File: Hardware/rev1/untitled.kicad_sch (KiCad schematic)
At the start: 16 parts, among them J2 USB_C_Receptacle_USB2.0_14P, J3 Screw_Terminal_01x02, U2 HT75xx-1-SOT89

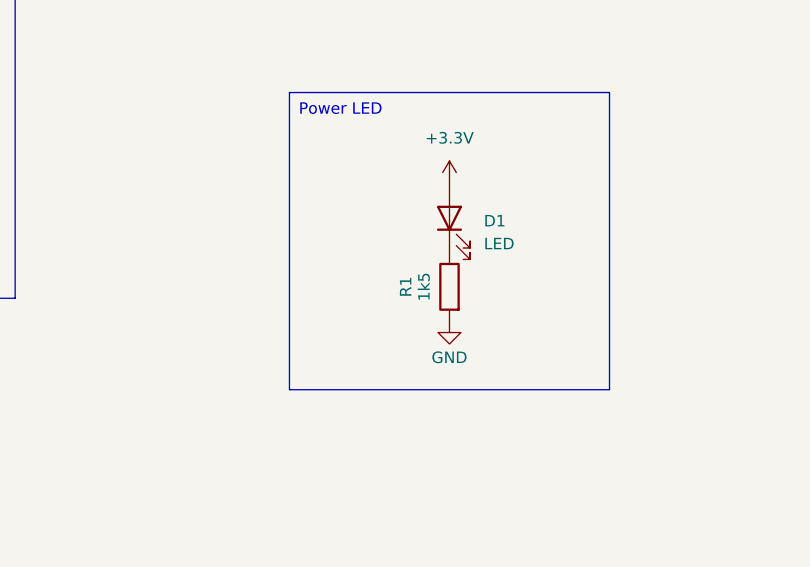
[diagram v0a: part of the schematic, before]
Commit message: Finish schematics, assign footprints
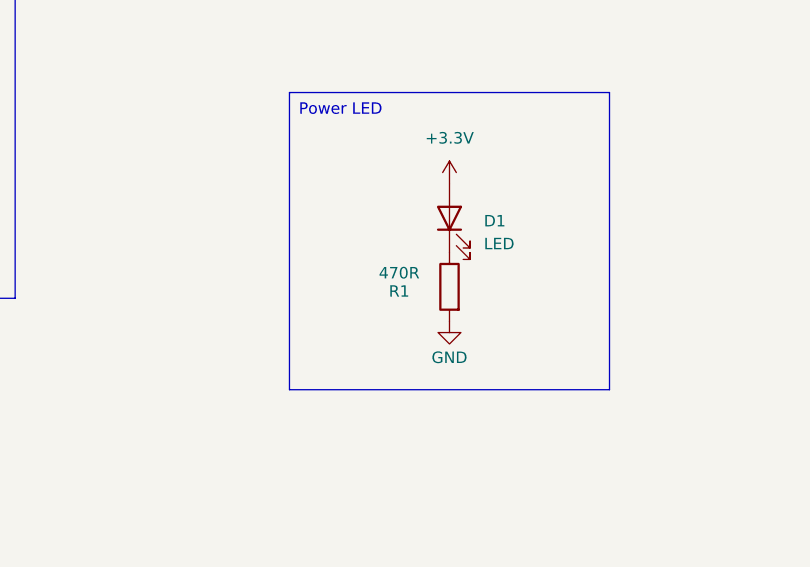
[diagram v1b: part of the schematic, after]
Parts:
- BT1: footprint (none) -> Battery:BatteryHolder_Keystone_3034_1x20mm
- C10, C8, C9: footprint (none) -> Capacitor_SMD:C_0603_1608Metric
- C7: footprint (none) -> Capacitor_SMD:C_0402_1005Metric
- D1: footprint (none) -> LED_SMD:LED_0201_0603Metric
- D2, D3: footprint (none) -> Diode_SMD:D_SOD-123F
- J2: footprint (none) -> Connector_USB:USB_C_Receptacle_HRO_TYPE-C-31-M-12
- J3: footprint (none) -> TerminalBlock:TerminalBlock_Xinya_XY308-2.54-2P_1x02_P2.54mm_Horizontal
- NT1: footprint (none) -> NetTie:NetTie-2_SMD_Pad2.0mm
- R1: value 1k5 -> 470R; footprint Resistor_SMD:R_0402_1005Metric -> Resistor_SMD:R_0603_1608Metric
- R3, R4, R5: footprint Resistor_SMD:R_0402_1005Metric -> Resistor_SMD:R_0603_1608Metric
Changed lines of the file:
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@@
 			)
 		)
-		(property "Footprint" "Resistor_SMD:R_0402_1005Metric"
+		(property "Footprint" "Resistor_SMD:R_0603_1608Metric"
 			(at 70.358 72.39 90)
 			(effects
@@
 			)
 		)
-		(property "Footprint" ""
+		(property "Footprint" "LED_SMD:LED_0201_0603Metric"
 			(at 151.13 90.17 0)
 			(effects
@@
 			)
 		)
-		(property "Footprint" ""
+		(property "Footprint" "Capacitor_SMD:C_0603_1608Metric"
 			(at 79.7052 163.83 0)
 			(effects
@@
 			)
 		)
-		(property "Footprint" ""
+		(property "Footprint" "Capacitor_SMD:C_0603_1608Metric"
 			(at 239.7252 100.33 0)
 			(effects
@@
 			)
 		)
-		(property "Footprint" ""
+		(property "Footprint" "NetTie:NetTie-2_SMD_Pad2.0mm"
 			(at 222.25 92.71 0)
 			(effects
@@
 			)
 		)
-		(property "Footprint" ""
+		(property "Footprint" "Diode_SMD:D_SOD-123F"
 			(at 50.8 135.89 0)
 			(effects
@@
 		(dnp no)
 		(property "Reference" "R1"
-			(at 146.304 97.79 90)
-			(effects
-				(font
-					(size 1.27 1.27)
-				)
-			)
-		)
-		(property "Value" "1k5"
-			(at 148.336 97.79 90)
-			(effects
-				(font
-					(size 1.27 1.27)
-				)
-			)
-		)
-		(property "Footprint" "Resistor_SMD:R_0402_1005Metric"
+			(at 145.542 98.298 0)
+			(effects
+				(font
+					(size 1.27 1.27)
+				)
+			)
+		)
+		(property "Value" "470R"
+			(at 145.542 96.266 0)
+			(effects
+				(font
+					(size 1.27 1.27)
+				)
+			)
+		)
+		(property "Footprint" "Resistor_SMD:R_0603_1608Metric"
 			(at 152.908 97.79 90)
 			(effects
@@
 			)
 		)
-		(property "Footprint" ""
+		(property "Footprint" "Capacitor_SMD:C_0402_1005Metric"
 			(at 230.8352 100.33 0)
 			(effects
@@
 			)
 		)
-		(property "Footprint" ""
+		(property "Footprint" "TerminalBlock:TerminalBlock_Xinya_XY308-2.54-2P_1x02_P2.54mm_Horizontal"
 			(at 68.58 139.7 0)
 			(effects
@@
 			)
 		)
-		(property "Footprint" ""
+		(property "Footprint" "Diode_SMD:D_SOD-123F"
 			(at 60.96 135.89 0)
 			(effects
@@
 			)
 		)
-		(property "Footprint" ""
+		(property "Footprint" "Battery:BatteryHolder_Keystone_3034_1x20mm"
 			(at 147.574 41.91 90)
 			(effects
@@
 			)
 		)
-		(property "Footprint" "Resistor_SMD:R_0402_1005Metric"
+		(property "Footprint" "Resistor_SMD:R_0603_1608Metric"
 			(at 81.28 52.578 90)
 			(effects
@@
 			)
 		)
-		(property "Footprint" "Resistor_SMD:R_0402_1005Metric"
+		(property "Footprint" "Resistor_SMD:R_0603_1608Metric"
 			(at 81.28 51.562 90)
 			(effects
@@
 			)
 		)
-		(property "Footprint" ""
+		(property "Footprint" "Connector_USB:USB_C_Receptacle_HRO_TYPE-C-31-M-12"
 			(at 55.88 60.96 0)
 			(effects
@@
 			)
 		)
-		(property "Footprint" ""
+		(property "Footprint" "Capacitor_SMD:C_0603_1608Metric"
 			(at 49.2252 163.83 0)
 			(effects

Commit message: Revert "Merge remote-tracking branch 'origin/dev'"
This reverts commit 9d6b38d1428df59ab2602e839e1db75647d3fbc2, reversing
changes made to aa461fd2fa90bcdcb689545e3dbed326723346fe.
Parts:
- BT1: footprint Battery:BatteryHolder_Keystone_3034_1x20mm -> (none)
- C10, C8, C9: footprint Capacitor_SMD:C_0603_1608Metric -> (none)
- C7: footprint Capacitor_SMD:C_0402_1005Metric -> (none)
- D1: footprint LED_SMD:LED_0201_0603Metric -> (none)
- D2, D3: footprint Diode_SMD:D_SOD-123F -> (none)
- J2: footprint Connector_USB:USB_C_Receptacle_HRO_TYPE-C-31-M-12 -> (none)
- J3: footprint TerminalBlock:TerminalBlock_Xinya_XY308-2.54-2P_1x02_P2.54mm_Horizontal -> (none)
- NT1: footprint NetTie:NetTie-2_SMD_Pad2.0mm -> (none)
- R1: value 470R -> 1k5; footprint Resistor_SMD:R_0603_1608Metric -> Resistor_SMD:R_0402_1005Metric
- R3, R4, R5: footprint Resistor_SMD:R_0603_1608Metric -> Resistor_SMD:R_0402_1005Metric
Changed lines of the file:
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@@
 			)
 		)
-		(property "Footprint" "Resistor_SMD:R_0603_1608Metric"
+		(property "Footprint" "Resistor_SMD:R_0402_1005Metric"
 			(at 70.358 72.39 90)
 			(effects
@@
 			)
 		)
-		(property "Footprint" "LED_SMD:LED_0201_0603Metric"
+		(property "Footprint" ""
 			(at 151.13 90.17 0)
 			(effects
@@
 			)
 		)
-		(property "Footprint" "Capacitor_SMD:C_0603_1608Metric"
+		(property "Footprint" ""
 			(at 79.7052 163.83 0)
 			(effects
@@
 			)
 		)
-		(property "Footprint" "Capacitor_SMD:C_0603_1608Metric"
+		(property "Footprint" ""
 			(at 239.7252 100.33 0)
 			(effects
@@
 			)
 		)
-		(property "Footprint" "NetTie:NetTie-2_SMD_Pad2.0mm"
+		(property "Footprint" ""
 			(at 222.25 92.71 0)
 			(effects
@@
 			)
 		)
-		(property "Footprint" "Diode_SMD:D_SOD-123F"
+		(property "Footprint" ""
 			(at 50.8 135.89 0)
 			(effects
@@
 		(dnp no)
 		(property "Reference" "R1"
-			(at 145.542 98.298 0)
-			(effects
-				(font
-					(size 1.27 1.27)
-				)
-			)
-		)
-		(property "Value" "470R"
-			(at 145.542 96.266 0)
-			(effects
-				(font
-					(size 1.27 1.27)
-				)
-			)
-		)
-		(property "Footprint" "Resistor_SMD:R_0603_1608Metric"
+			(at 146.304 97.79 90)
+			(effects
+				(font
+					(size 1.27 1.27)
+				)
+			)
+		)
+		(property "Value" "1k5"
+			(at 148.336 97.79 90)
+			(effects
+				(font
+					(size 1.27 1.27)
+				)
+			)
+		)
+		(property "Footprint" "Resistor_SMD:R_0402_1005Metric"
 			(at 152.908 97.79 90)
 			(effects
@@
 			)
 		)
-		(property "Footprint" "Capacitor_SMD:C_0402_1005Metric"
+		(property "Footprint" ""
 			(at 230.8352 100.33 0)
 			(effects
@@
 			)
 		)
-		(property "Footprint" "TerminalBlock:TerminalBlock_Xinya_XY308-2.54-2P_1x02_P2.54mm_Horizontal"
+		(property "Footprint" ""
 			(at 68.58 139.7 0)
 			(effects
@@
 			)
 		)
-		(property "Footprint" "Diode_SMD:D_SOD-123F"
+		(property "Footprint" ""
 			(at 60.96 135.89 0)
 			(effects
@@
 			)
 		)
-		(property "Footprint" "Battery:BatteryHolder_Keystone_3034_1x20mm"
+		(property "Footprint" ""
 			(at 147.574 41.91 90)
 			(effects
@@
 			)
 		)
-		(property "Footprint" "Resistor_SMD:R_0603_1608Metric"
+		(property "Footprint" "Resistor_SMD:R_0402_1005Metric"
 			(at 81.28 52.578 90)
 			(effects
@@
 			)
 		)
-		(property "Footprint" "Resistor_SMD:R_0603_1608Metric"
+		(property "Footprint" "Resistor_SMD:R_0402_1005Metric"
 			(at 81.28 51.562 90)
 			(effects
@@
 			)
 		)
-		(property "Footprint" "Connector_USB:USB_C_Receptacle_HRO_TYPE-C-31-M-12"
+		(property "Footprint" ""
 			(at 55.88 60.96 0)
 			(effects
@@
 			)
 		)
-		(property "Footprint" "Capacitor_SMD:C_0603_1608Metric"
+		(property "Footprint" ""
 			(at 49.2252 163.83 0)
 			(effects
